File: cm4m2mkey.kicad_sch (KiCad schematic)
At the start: 26 parts, among them J8 1-2199119-6

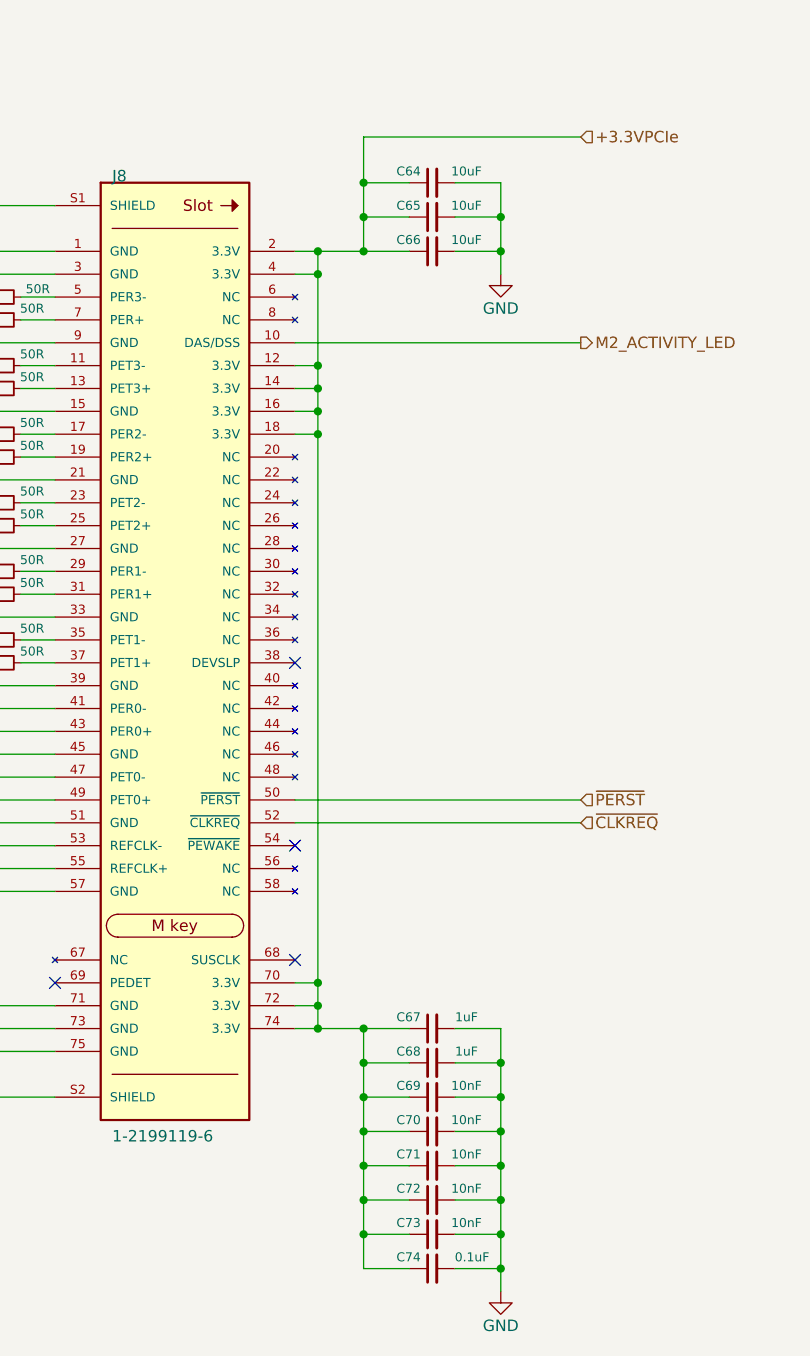
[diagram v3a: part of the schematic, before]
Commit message: initial integration of i2c arbiter
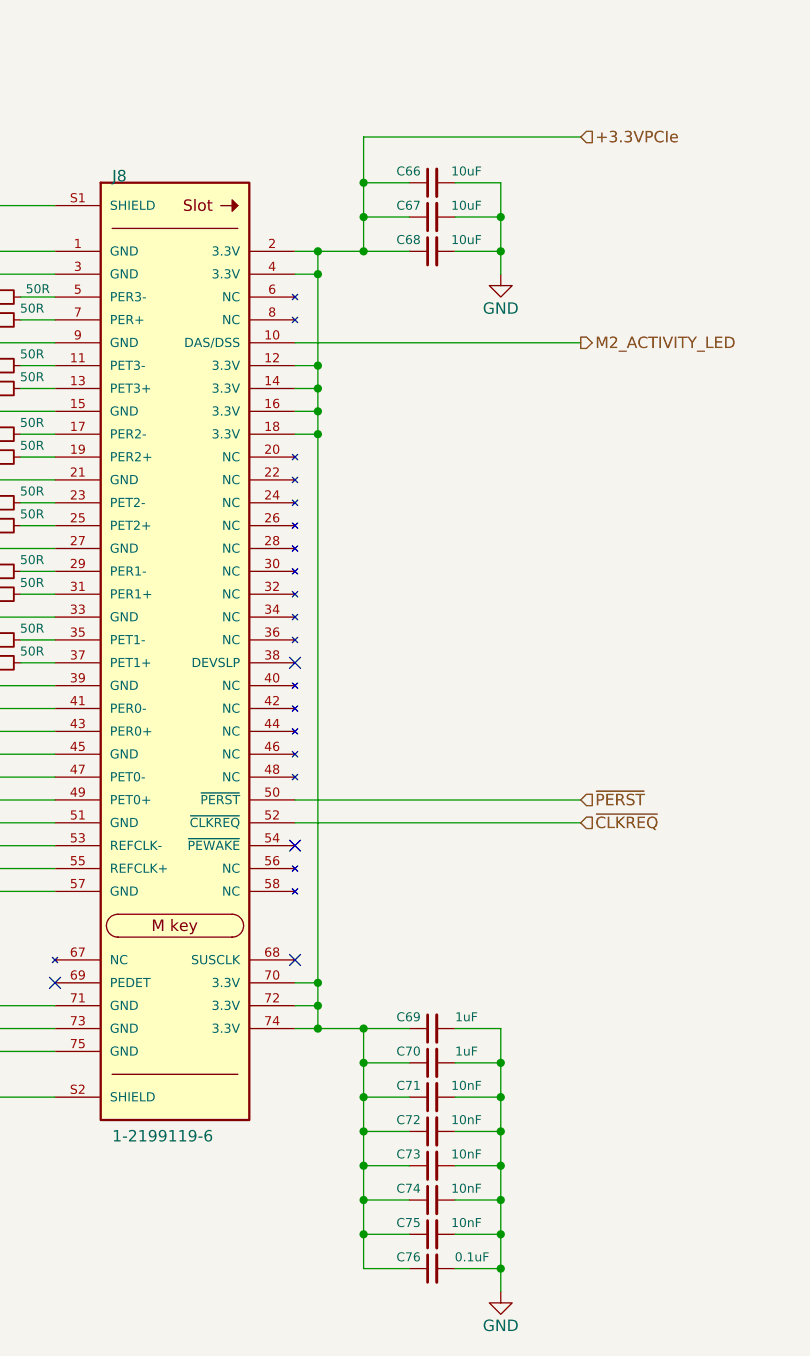
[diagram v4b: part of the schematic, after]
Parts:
- renumbered C64 to C66, C65 to C67, C66 to C68, C67 to C69, C68 to C70, C69 to C71, C70 to C72, C71 to C73, C72 to C74, C73 to C75, C74 to C76
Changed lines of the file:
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@@
   (symbol (lib_id "Device:C_Small") (at 147.32 54.61 90) (unit 1)
     (in_bom yes) (on_board yes)
-    (property "Reference" "C66" (id 0) (at 146.05 53.34 90)
+    (property "Reference" "C68" (id 0) (at 146.05 53.34 90)
       (effects (font (size 1 1)) (justify left))
     )
@@
   (symbol (lib_id "Device:C_Small") (at 147.32 167.64 90) (unit 1)
     (in_bom yes) (on_board yes)
-    (property "Reference" "C74" (id 0) (at 146.05 166.37 90)
+    (property "Reference" "C76" (id 0) (at 146.05 166.37 90)
       (effects (font (size 1 1)) (justify left))
     )
@@
   (symbol (lib_id "Device:C_Small") (at 147.32 152.4 90) (unit 1)
     (in_bom yes) (on_board yes)
-    (property "Reference" "C70" (id 0) (at 146.05 151.13 90)
+    (property "Reference" "C72" (id 0) (at 146.05 151.13 90)
       (effects (font (size 1 1)) (justify left))
     )
@@
   (symbol (lib_id "Device:C_Small") (at 147.32 144.78 90) (unit 1)
     (in_bom yes) (on_board yes)
-    (property "Reference" "C68" (id 0) (at 146.05 143.51 90)
+    (property "Reference" "C70" (id 0) (at 146.05 143.51 90)
       (effects (font (size 1 1)) (justify left))
     )
@@
   (symbol (lib_id "Device:C_Small") (at 147.32 140.97 90) (unit 1)
     (in_bom yes) (on_board yes)
-    (property "Reference" "C67" (id 0) (at 146.05 139.7 90)
+    (property "Reference" "C69" (id 0) (at 146.05 139.7 90)
       (effects (font (size 1 1)) (justify left))
     )
@@
   (symbol (lib_id "Device:C_Small") (at 147.32 148.59 90) (unit 1)
     (in_bom yes) (on_board yes)
-    (property "Reference" "C69" (id 0) (at 146.05 147.32 90)
+    (property "Reference" "C71" (id 0) (at 146.05 147.32 90)
       (effects (font (size 1 1)) (justify left))
     )
@@
   (symbol (lib_id "Device:C_Small") (at 147.32 46.99 90) (unit 1)
     (in_bom yes) (on_board yes)
-    (property "Reference" "C64" (id 0) (at 146.05 45.72 90)
+    (property "Reference" "C66" (id 0) (at 146.05 45.72 90)
       (effects (font (size 1 1)) (justify left))
     )
@@
   (symbol (lib_id "power:GND") (at 90.17 153.67 0) (unit 1)
     (in_bom yes) (on_board yes)
-    (property "Reference" "#PWR054" (id 0) (at 90.17 160.02 0)
+    (property "Reference" "#PWR055" (id 0) (at 90.17 160.02 0)
       (effects (font (size 1.27 1.27)) hide)
     )
@@
   (symbol (lib_id "power:GND") (at 154.94 170.18 0) (unit 1)
     (in_bom yes) (on_board yes)
-    (property "Reference" "#PWR056" (id 0) (at 154.94 176.53 0)
+    (property "Reference" "#PWR057" (id 0) (at 154.94 176.53 0)
       (effects (font (size 1.27 1.27)) hide)
     )
@@
   (symbol (lib_id "Device:C_Small") (at 147.32 163.83 90) (unit 1)
     (in_bom yes) (on_board yes)
-    (property "Reference" "C73" (id 0) (at 146.05 162.56 90)
+    (property "Reference" "C75" (id 0) (at 146.05 162.56 90)
       (effects (font (size 1 1)) (justify left))
     )
@@
   (symbol (lib_id "Device:C_Small") (at 147.32 156.21 90) (unit 1)
     (in_bom yes) (on_board yes)
-    (property "Reference" "C71" (id 0) (at 146.05 154.94 90)
+    (property "Reference" "C73" (id 0) (at 146.05 154.94 90)
       (effects (font (size 1 1)) (justify left))
     )
@@
   (symbol (lib_id "power:GND") (at 154.94 57.15 0) (unit 1)
     (in_bom yes) (on_board yes)
-    (property "Reference" "#PWR055" (id 0) (at 154.94 63.5 0)
+    (property "Reference" "#PWR056" (id 0) (at 154.94 63.5 0)
       (effects (font (size 1.27 1.27)) hide)
     )
@@
   (symbol (lib_id "Device:C_Small") (at 147.32 50.8 90) (unit 1)
     (in_bom yes) (on_board yes)
-    (property "Reference" "C65" (id 0) (at 146.05 49.53 90)
+    (property "Reference" "C67" (id 0) (at 146.05 49.53 90)
       (effects (font (size 1 1)) (justify left))
     )
@@
   (symbol (lib_id "Device:C_Small") (at 147.32 160.02 90) (unit 1)
     (in_bom yes) (on_board yes)
-    (property "Reference" "C72" (id 0) (at 146.05 158.75 90)
-      (effects (font (size 1 1)) (justify left))
-    )
+    (property "Reference" "C74" (id 0) (at 146.05 158.75 90)
+      (effects (font (size 1 1)) (justify left))
+    )

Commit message: footprint assignment
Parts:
- renumbered C66 to C68, C67 to C69, C68 to C70, C69 to C71, C70 to C72, C71 to C73, C72 to C74, C73 to C75, C74 to C76, C75 to C77, C76 to C78, R55 to R61, R56 to R62, R57 to R63, R58 to R64, R59 to R65, R60 to R66, R61 to R67, R62 to R68, R63 to R69, R64 to R70, R65 to R71, R66 to R72, R67 to R73, R68 to R74
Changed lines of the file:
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@@
   (symbol (lib_id "Device:R_Small") (at 81.28 118.11 90) (unit 1)
     (in_bom yes) (on_board yes)
-    (property "Reference" "R55" (id 0) (at 74.93 116.84 90)
+    (property "Reference" "R61" (id 0) (at 74.93 116.84 90)
       (effects (font (size 1 1)) (justify right))
     )
@@
   (symbol (lib_id "Device:R_Small") (at 99.06 77.47 90) (unit 1)
     (in_bom yes) (on_board yes)
-    (property "Reference" "R62" (id 0) (at 92.71 76.2 90)
+    (property "Reference" "R68" (id 0) (at 92.71 76.2 90)
       (effects (font (size 1 1)) (justify right))
     )
@@
   (symbol (lib_id "Device:C_Small") (at 147.32 54.61 90) (unit 1)
     (in_bom yes) (on_board yes)
-    (property "Reference" "C68" (id 0) (at 146.05 53.34 90)
+    (property "Reference" "C70" (id 0) (at 146.05 53.34 90)
       (effects (font (size 1 1)) (justify left))
     )
@@
   (symbol (lib_id "Device:R_Small") (at 99.06 82.55 90) (unit 1)
     (in_bom yes) (on_board yes)
-    (property "Reference" "R63" (id 0) (at 92.71 81.28 90)
+    (property "Reference" "R69" (id 0) (at 92.71 81.28 90)
       (effects (font (size 1 1)) (justify right))
     )
@@
   (symbol (lib_id "Device:C_Small") (at 147.32 167.64 90) (unit 1)
     (in_bom yes) (on_board yes)
-    (property "Reference" "C76" (id 0) (at 146.05 166.37 90)
+    (property "Reference" "C78" (id 0) (at 146.05 166.37 90)
       (effects (font (size 1 1)) (justify left))
     )
@@
   (symbol (lib_id "Device:R_Small") (at 99.06 74.93 90) (unit 1)
     (in_bom yes) (on_board yes)
-    (property "Reference" "R61" (id 0) (at 92.71 73.66 90)
+    (property "Reference" "R67" (id 0) (at 92.71 73.66 90)
       (effects (font (size 1 1)) (justify right))
     )
@@
   (symbol (lib_id "Device:R_Small") (at 99.06 59.69 90) (unit 1)
     (in_bom yes) (on_board yes)
-    (property "Reference" "R57" (id 0) (at 93.345 58.801 90)
+    (property "Reference" "R63" (id 0) (at 93.345 58.801 90)
       (effects (font (size 1 1)) (justify right))
     )
@@
   (symbol (lib_id "Device:R_Small") (at 99.06 67.31 90) (unit 1)
     (in_bom yes) (on_board yes)
-    (property "Reference" "R59" (id 0) (at 92.71 66.04 90)
+    (property "Reference" "R65" (id 0) (at 92.71 66.04 90)
       (effects (font (size 1 1)) (justify right))
     )
@@
   (symbol (lib_id "Device:C_Small") (at 147.32 152.4 90) (unit 1)
     (in_bom yes) (on_board yes)
-    (property "Reference" "C72" (id 0) (at 146.05 151.13 90)
+    (property "Reference" "C74" (id 0) (at 146.05 151.13 90)
       (effects (font (size 1 1)) (justify left))
     )
@@
   (symbol (lib_id "Device:C_Small") (at 147.32 144.78 90) (unit 1)
     (in_bom yes) (on_board yes)
-    (property "Reference" "C70" (id 0) (at 146.05 143.51 90)
+    (property "Reference" "C72" (id 0) (at 146.05 143.51 90)
       (effects (font (size 1 1)) (justify left))
     )
@@
   (symbol (lib_id "Device:C_Small") (at 147.32 140.97 90) (unit 1)
     (in_bom yes) (on_board yes)
-    (property "Reference" "C69" (id 0) (at 146.05 139.7 90)
+    (property "Reference" "C71" (id 0) (at 146.05 139.7 90)
       (effects (font (size 1 1)) (justify left))
     )
@@
   (symbol (lib_id "Device:R_Small") (at 99.06 97.79 90) (unit 1)
     (in_bom yes) (on_board yes)
-    (property "Reference" "R67" (id 0) (at 92.71 96.52 90)
+    (property "Reference" "R73" (id 0) (at 92.71 96.52 90)
       (effects (font (size 1 1)) (justify right))
     )
@@
   (symbol (lib_id "Device:C_Small") (at 147.32 148.59 90) (unit 1)
     (in_bom yes) (on_board yes)
-    (property "Reference" "C71" (id 0) (at 146.05 147.32 90)
+    (property "Reference" "C73" (id 0) (at 146.05 147.32 90)
       (effects (font (size 1 1)) (justify left))
     )
@@
   (symbol (lib_id "Device:C_Small") (at 147.32 46.99 90) (unit 1)
     (in_bom yes) (on_board yes)
-    (property "Reference" "C66" (id 0) (at 146.05 45.72 90)
+    (property "Reference" "C68" (id 0) (at 146.05 45.72 90)
       (effects (font (size 1 1)) (justify left))
     )
@@
   (symbol (lib_id "power:GND") (at 90.17 153.67 0) (unit 1)
     (in_bom yes) (on_board yes)
-    (property "Reference" "#PWR055" (id 0) (at 90.17 160.02 0)
+    (property "Reference" "#PWR057" (id 0) (at 90.17 160.02 0)
       (effects (font (size 1.27 1.27)) hide)
     )
@@
   (symbol (lib_id "power:GND") (at 154.94 170.18 0) (unit 1)
     (in_bom yes) (on_board yes)
-    (property "Reference" "#PWR057" (id 0) (at 154.94 176.53 0)
+    (property "Reference" "#PWR059" (id 0) (at 154.94 176.53 0)
       (effects (font (size 1.27 1.27)) hide)
     )
@@
   (symbol (lib_id "Device:R_Small") (at 99.06 69.85 90) (unit 1)
     (in_bom yes) (on_board yes)
-    (property "Reference" "R60" (id 0) (at 92.71 68.58 90)
+    (property "Reference" "R66" (id 0) (at 92.71 68.58 90)
       (effects (font (size 1 1)) (justify right))
     )
@@
   (symbol (lib_id "Device:C_Small") (at 147.32 163.83 90) (unit 1)
     (in_bom yes) (on_board yes)
-    (property "Reference" "C75" (id 0) (at 146.05 162.56 90)
+    (property "Reference" "C77" (id 0) (at 146.05 162.56 90)
       (effects (font (size 1 1)) (justify left))
     )
@@
   (symbol (lib_id "Device:C_Small") (at 147.32 156.21 90) (unit 1)
     (in_bom yes) (on_board yes)
-    (property "Reference" "C73" (id 0) (at 146.05 154.94 90)
+    (property "Reference" "C75" (id 0) (at 146.05 154.94 90)
       (effects (font (size 1 1)) (justify left))
     )
@@
   (symbol (lib_id "power:GND") (at 154.94 57.15 0) (unit 1)
     (in_bom yes) (on_board yes)
-    (property "Reference" "#PWR056" (id 0) (at 154.94 63.5 0)
+    (property "Reference" "#PWR058" (id 0) (at 154.94 63.5 0)
       (effects (font (size 1.27 1.27)) hide)
     )
@@
   (symbol (lib_id "Device:R_Small") (at 99.06 90.17 90) (unit 1)
     (in_bom yes) (on_board yes)
-    (property "Reference" "R65" (id 0) (at 92.71 88.9 90)
+    (property "Reference" "R71" (id 0) (at 92.71 88.9 90)
       (effects (font (size 1 1)) (justify right))
     )
@@
   (symbol (lib_id "Device:R_Small") (at 99.06 62.23 90) (unit 1)
     (in_bom yes) (on_board yes)
-    (property "Reference" "R58" (id 0) (at 92.71 60.96 90)
+    (property "Reference" "R64" (id 0) (at 92.71 60.96 90)
       (effects (font (size 1 1)) (justify right))
     )
@@
   (symbol (lib_id "Device:C_Small") (at 147.32 50.8 90) (unit 1)
     (in_bom yes) (on_board yes)
-    (property "Reference" "C67" (id 0) (at 146.05 49.53 90)
+    (property "Reference" "C69" (id 0) (at 146.05 49.53 90)
       (effects (font (size 1 1)) (justify left))
     )
@@
   (symbol (lib_id "Device:R_Small") (at 81.28 125.73 90) (unit 1)
     (in_bom yes) (on_board yes)
-    (property "Reference" "R56" (id 0) (at 74.93 127 90)
+    (property "Reference" "R62" (id 0) (at 74.93 127 90)
       (effects (font (size 1 1)) (justify right))
     )
@@
   (symbol (lib_id "Device:R_Small") (at 99.06 100.33 90) (unit 1)
     (in_bom yes) (on_board yes)
-    (property "Reference" "R68" (id 0) (at 92.71 99.06 90)
+    (property "Reference" "R74" (id 0) (at 92.71 99.06 90)
       (effects (font (size 1 1)) (justify right))
     )
@@
   (symbol (lib_id "Device:C_Small") (at 147.32 160.02 90) (unit 1)
     (in_bom yes) (on_board yes)
-    (property "Reference" "C74" (id 0) (at 146.05 158.75 90)
+    (property "Reference" "C76" (id 0) (at 146.05 158.75 90)
       (effects (font (size 1 1)) (justify left))
     )
@@
   (symbol (lib_id "Device:R_Small") (at 99.06 85.09 90) (unit 1)
     (in_bom yes) (on_board yes)
-    (property "Reference" "R64" (id 0) (at 92.71 83.82 90)
+    (property "Reference" "R70" (id 0) (at 92.71 83.82 90)
       (effects (font (size 1 1)) (justify right))
     )
@@
   (symbol (lib_id "Device:R_Small") (at 99.06 92.71 90) (unit 1)
     (in_bom yes) (on_board yes)
-    (property "Reference" "R66" (id 0) (at 92.71 91.44 90)
-      (effects (font (size 1 1)) (justify right))
-    )
+    (property "Reference" "R72" (id 0) (at 92.71 91.44 90)
+      (effects (font (size 1 1)) (justify right))
+    )
